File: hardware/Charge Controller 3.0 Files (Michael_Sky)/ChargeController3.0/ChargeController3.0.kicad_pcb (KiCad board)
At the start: 2 copper layers, 95.9 x 90.2 mm, 98 parts, among them J1 Conn_02x26_Odd_Even, J1 Conn_02x30_Row_Letter_First, J10 SOL_TEST_01x01_Pin, J11 GND_TEST_01x01_Pin, J12 Conn_02x26_Odd_Even, J13 Conn-1x2, J14 Conn-1x2, J15 Conn-1x2, J17 SCL_MAS_01x01_Pin, J18 SDA_MAS_01x01_Pin, J19 SYS-1x2, J2 Conn_02x30_Row_Letter_First, J2 SP_01x02_Pin, J3 BATT_TEST_01x01_Pin, J4 3.3V_PULLUP_01x02_Pin, J5 BATT_01x02_Pin, J6 Conn-1x2, J7 Conn-1x2, J8 Conn-1x2, J9 SYS_TEST_01x01_Pin, Q1 SI2318CDS-T1-GE3, Q10 SI2318CDS-T1-GE3, Q11 SI2318CDS-T1-GE3, Q13 SI2318CDS-T1-GE3, Q2 SI2318CDS-T1-GE3, Q3 SI2318CDS-T1-GE3, Q4 SI2318CDS-T1-GE3, Q5 AONS66614, Q6 AONS66614, Q7 AONS66614, Q8 AONS66614, Q9 SI2318CDS-T1-GE3, SW1 100SP1T1B1M1QEH, U1 BQ25756ERRVR

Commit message: template layout
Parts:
- removed D6: SS24, bmsfootprints:SS24
- removed the H1 at (38.6, 3.02)
- removed the H1 at (102.8, 59.0)
- removed the H2 at (38.6, 10.1)
- removed the H2 at (188.5, 56.5)
- removed the H3 at (38.6, 17.1)
- removed the H3 at (102.8, 132.7)
- removed the H4 at (38.6, 24.2)
- removed the H4 at (188.5, 136.5)
- removed the J1 at (106.8, 125.1)
- removed the J1 at (73.0, 4.64)
- removed the J2 at (102.8, 125.1)
- removed the J2 at (15.3, 50.7)
- removed the J3 at (10.6, 41.7)
- removed the J4 at (32.4, 32.5)
- removed Q13: SI2318CDS-T1-GE3, bmsfootprints:SI2318CDS-T1-GE3
- added H1: MountingHole_Pad, MountingHole:MountingHole_3.2mm_M3_Pad_TopBottom, F.Cu at (113.6, 53.0)
- added H2: MountingHole_Pad, MountingHole:MountingHole_3.2mm_M3_Pad_TopBottom, F.Cu at (199.3, 56.8)
- added H3: MountingHole_Pad, MountingHole:MountingHole_3.2mm_M3_Pad_TopBottom, F.Cu at (113.6, 133.0)
- added H4: MountingHole_Pad, MountingHole:MountingHole_3.2mm_M3_Pad_TopBottom, F.Cu at (199.3, 130.5)
- added H4: MountingHole_Pad, MountingHole:MountingHole_3.2mm_M3_ISO14580_Pad, F.Cu at (36.3, 79.5)
- added J1: Conn_02x26_Odd_Even, Connector_PinSocket_2.54mm:PinSocket_2x26_P2.54mm_Vertical, F.Cu at (21.3, 18.3)
- added J2: SP_01x02_Pin, Connector_PinHeader_2.54mm:PinHeader_1x02_P2.54mm_Vertical, F.Cu at (49.3, 48.9)
- added J3: BATT_TEST_01x01_Pin, Connector_PinHeader_2.54mm:PinHeader_1x01_P2.54mm_Vertical, F.Cu at (53.7, 57.9)
- added J3: Conn_02x26_Row_Letter_First, Connector_PinSocket_2.54mm:PinSocket_2x26_P2.54mm_Vertical, F.Cu at (194.2, 61.9)
- added J4: Conn_02x26_Row_Letter_First, Connector_PinSocket_2.54mm:PinSocket_2x26_P2.54mm_Vertical, F.Cu at (199.3, 61.9)
- added J4: 3.3V_PULLUP_01x02_Pin, Connector_PinHeader_2.54mm:PinHeader_1x02_P2.54mm_Vertical, F.Cu at (65.1, 48.9)
- moved J6 76.1 mm to (65.1, 75.7)
- moved J7 76.1 mm to (69.7, 75.7)
- moved R24 76.1 mm to (74.5, 81.5)
- moved RT1 76.1 mm to (65.9, 82.4)
- moved R25 76.1 mm to (71.1, 81.8)
- moved R26 76.1 mm to (71.1, 84.3)
- moved J8 76.1 mm to (74.3, 75.7)
- moved J12 55.3 mm to (28.5, 18.3)
- moved D7 47.7 mm to (47.4, 58.2)
- moved D8 47.7 mm to (47.4, 63.4)
- moved D9 47.7 mm to (47.4, 68.6)
- moved J9 46.1 mm to (53.7, 62.5)
- moved J10 46.1 mm to (53.7, 67.1)
- moved J11 46.0 mm to (53.7, 71.7)
- moved Q4 39.8 mm to (35.2, 71.7)
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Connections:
- C12 pad 2: GND -> PGND
- C13 pad 2: GND -> PGND
- C14 pad 1: GND -> PGND
- C16 pad 1: GND -> PGND
- C17 pad 2: GND -> PGND
- C18 pad 2: GND -> PGND
- C2 pad 2: GND -> PGND
- C22 pad 2: GND -> PGND
- C23 pad 2: GND -> PGND
- C24 pad 2: GND -> PGND
- C25 pad 1: GND -> PGND
- C27 pad 1: GND -> PGND
- C3 pad 2: GND -> PGND
- C4 pad 2: GND -> PGND
- C6 pad 2: GND -> PGND
- C7 pad 2: GND -> PGND
- D7 pad A: Net-(D6-PadC) -> Net-(J10-Pin_1)
- J11 pad 1: GND -> PGND
- J12 pad 23: unconnected-(J12-Pin_23-Pad23) -> 3.3V
- J12 pad 24: unconnected-(J12-Pin_24-Pad24) -> 3.3V
- J12 pad 27: unconnected-(J12-Pin_27-Pad27) -> 12V
- J12 pad 28: unconnected-(J12-Pin_28-Pad28) -> 12V
- J12 pad 29: GND -> PGND
- J12 pad 30: GND -> PGND
- J12 pad 31: GND -> PGND
- J12 pad 32: GND -> PGND
- J12 pad 43: unconnected-(J12-Pin_43-Pad43) -> SOL
- J12 pad 45: BATT -> SYS/BATT
- J13 pad 1: GND -> PGND
- J19 pad 2: GND -> PGND
- J8 pad 2: GND -> PGND
- Q1 pad 3: Net-(D6-PadC) -> Net-(J10-Pin_1)
- Q7 pad 1: GND -> PGND
- Q7 pad 2: GND -> PGND
- Q7 pad 3: GND -> PGND
- Q8 pad 1: GND -> PGND
- Q8 pad 2: GND -> PGND
- Q8 pad 3: GND -> PGND
- Q9 pad 3: GND -> PGND
- R24 pad 1: GND -> PGND
- R26 pad 1: GND -> PGND
- R_AC3 pad 2: GND -> PGND
- R_FSW_SYNC1 pad 1: GND -> PGND
- R_ICHG1 pad 1: GND -> PGND
- R_ILIM_HIZ1 pad 1: GND -> PGND
- SW1 pad 3: GND -> PGND
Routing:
- added copper zone on B.Cu, net GND
- added copper zone on F.Cu, net GND

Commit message: pcb template start
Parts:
- removed the J3 at (194.2, 61.9)
- removed the J4 at (199.3, 61.9)
- moved J1 177.3 mm to (189.7, 73.9)
- moved J12 175.4 mm to (194.8, 73.9)
- moved L1 108.2 mm to (124.4, 105.5)
- moved H1 12.8 mm to (109.1, 65.0)
- moved H2 12.8 mm to (194.8, 68.8)
- moved H3 12.8 mm to (109.1, 145.0)
- moved H4 12.8 mm to (194.8, 142.5)
- moved Q1 8.34 mm to (26.9, 57.0)
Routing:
- removed copper zone on B.Cu, net GND
- removed copper zone on F.Cu, net GND
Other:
- board text removed: "A1"
- board text removed: "A30"
- board text removed: "B"
- board text removed: "C"
- board text removed: "D1"
- board text removed: "D30"

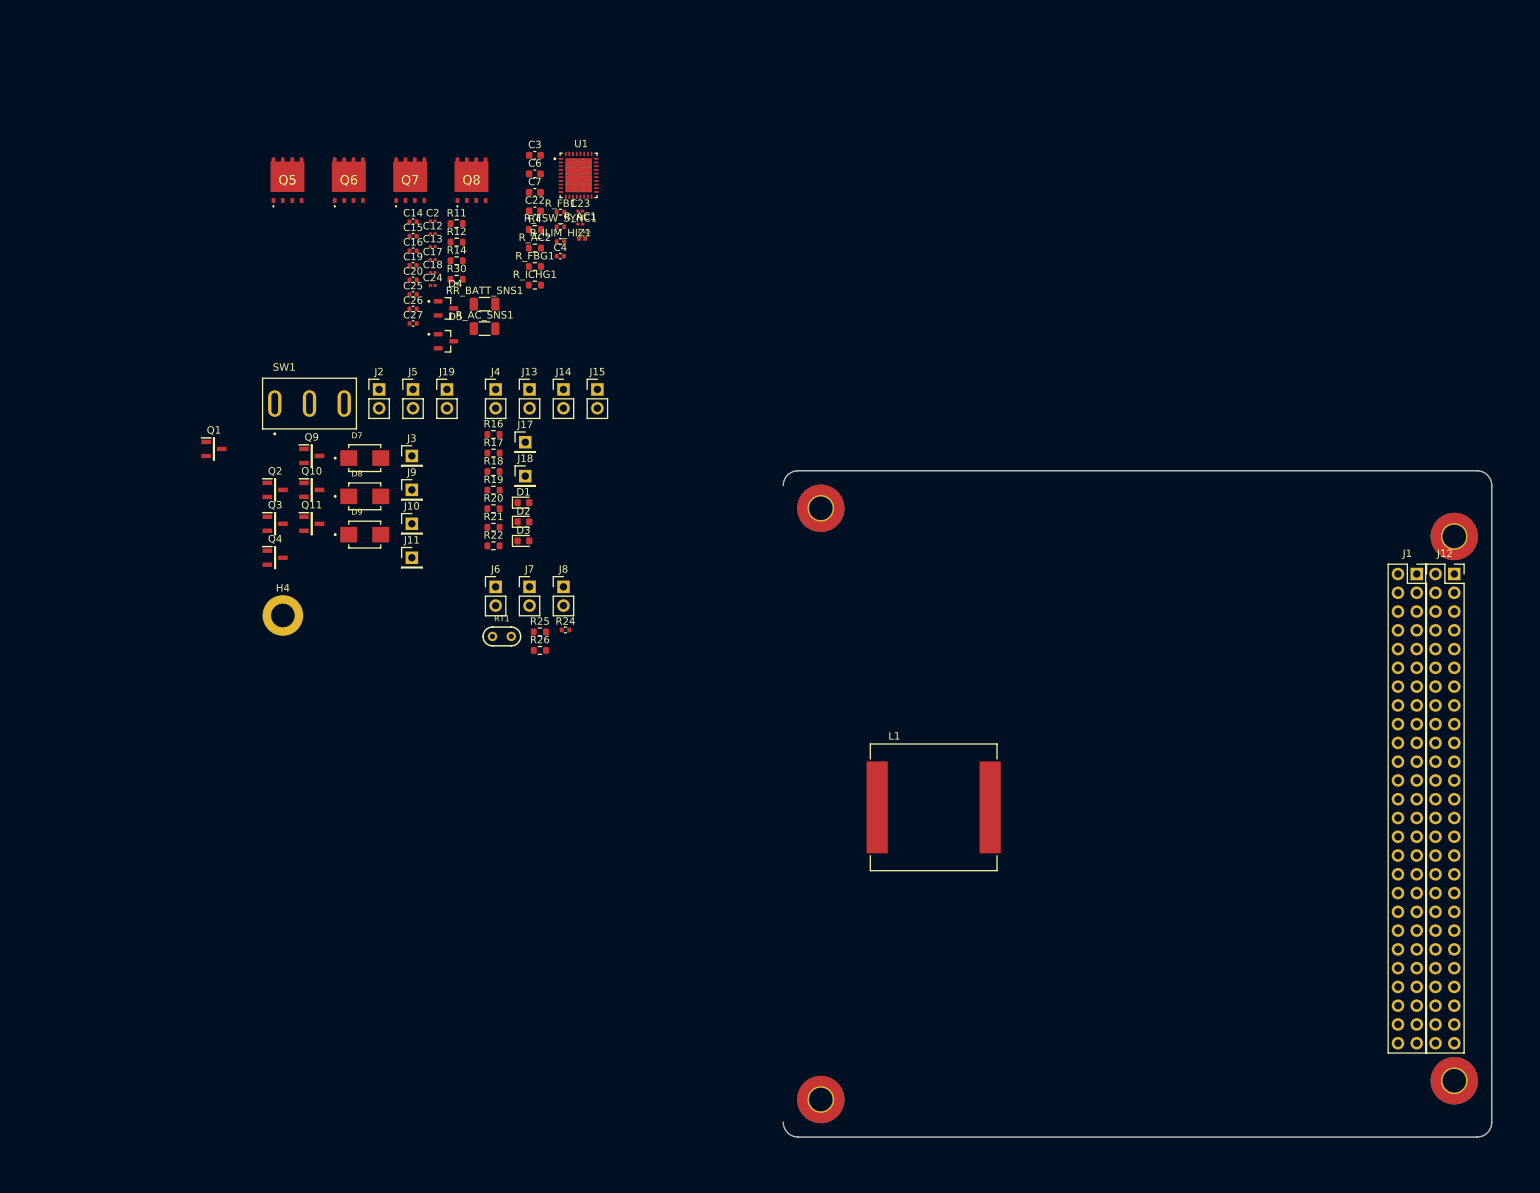
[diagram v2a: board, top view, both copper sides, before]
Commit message: Added template, reassigned pins
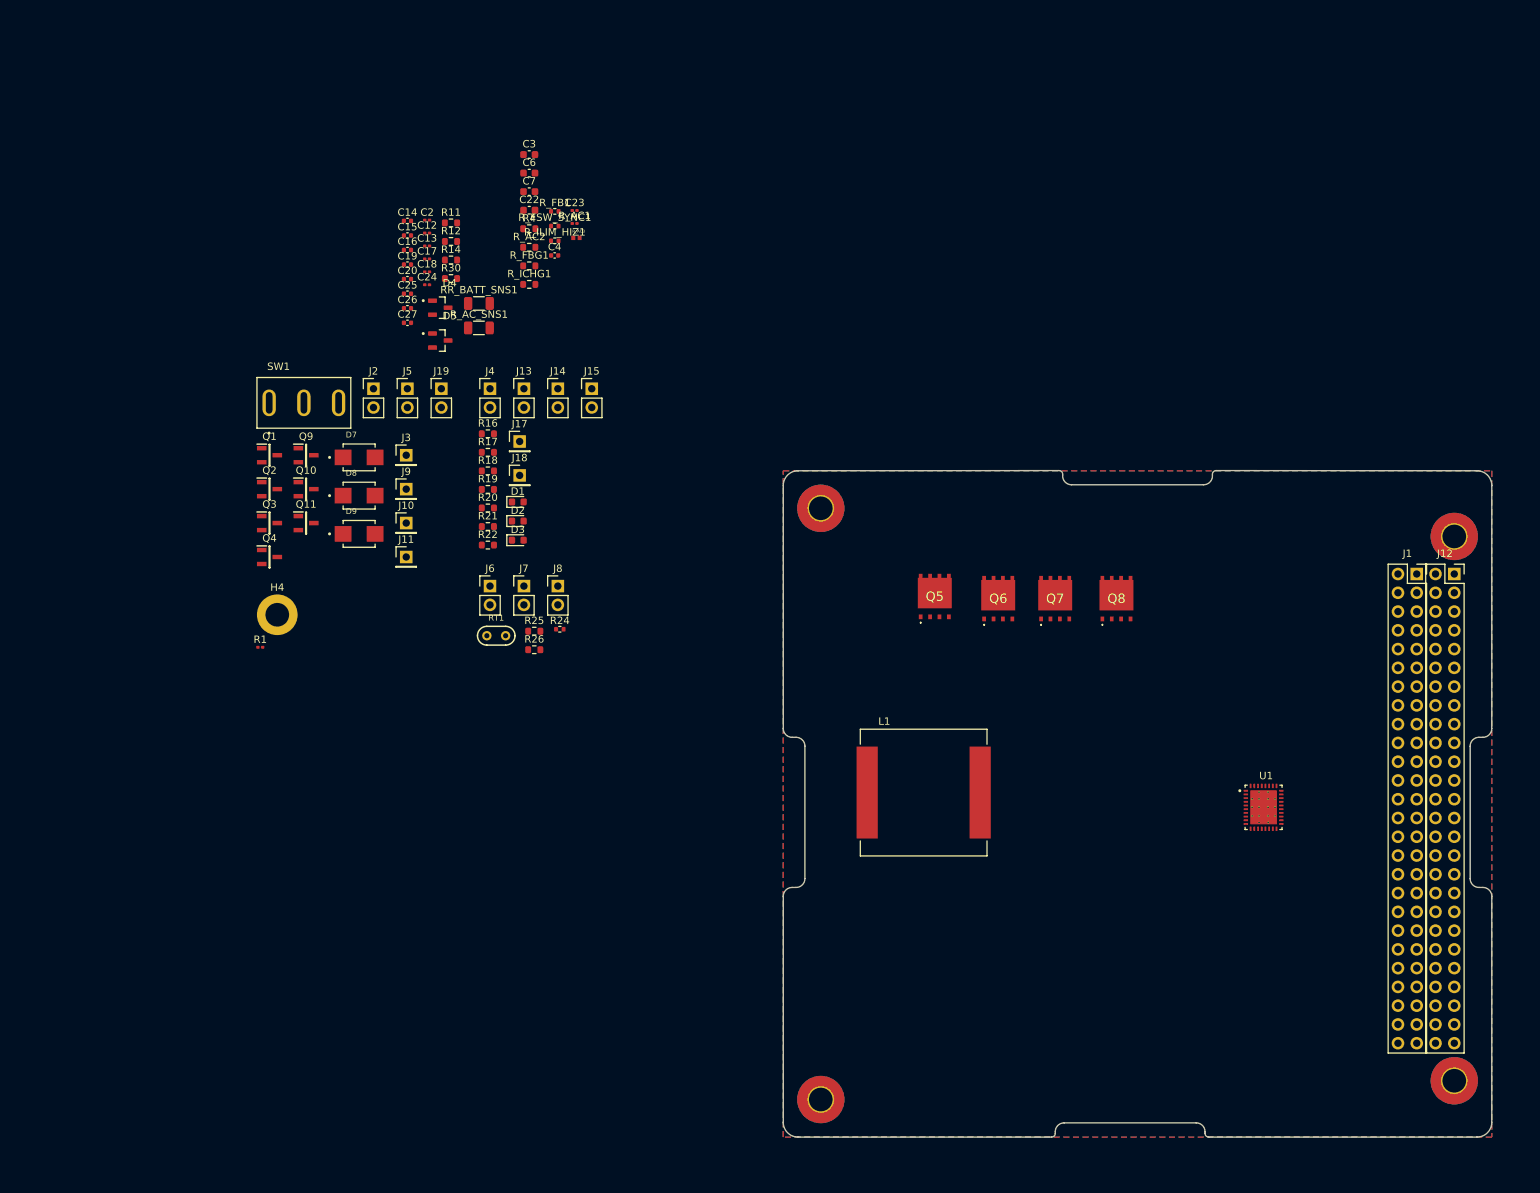
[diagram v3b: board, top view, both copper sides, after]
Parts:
- added R1: 1M, Resistor_SMD:R_0201_0603Metric, F.Cu at (33.2, 83.8)
- moved U1 126.1 mm to (169.0, 105.5)
- moved Q6 104.5 mm to (133.1, 77.2)
- moved Q5 104.1 mm to (124.5, 77.0)
- moved Q7 104.0 mm to (140.8, 77.2)
- moved Q8 104.0 mm to (149.1, 77.2)
- moved Q1 7.57 mm to (34.5, 57.8)
- moved L1 2.42 mm to (123.0, 103.5)
- moved R24 0.77 mm to (73.8, 81.4)
- moved RT1 0.77 mm to (65.2, 82.3)
- moved J13 0.77 mm to (68.9, 48.8)
- moved J4 0.77 mm to (64.3, 48.8)
- moved J5 0.77 mm to (53.1, 48.8)
- moved R_ICHG1 0.77 mm to (69.6, 34.7)
- moved C22 0.77 mm to (69.6, 24.7)
- moved C23 0.77 mm to (75.8, 24.7)
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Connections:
- J1 pad 22: unconnected-(J1-Pin_22-Pad22) -> RS-485 SYS1 B
- J1 pad 24: unconnected-(J1-Pin_24-Pad24) -> RS-485 SYS1 B
- J1 pad 39: unconnected-(J1-Pin_39-Pad39) -> RS SYS2 Rx
- J1 pad 40: unconnected-(J1-Pin_40-Pad40) -> RS SYS2 Tx
- J12 pad 23: 3.3V -> 12V
- J12 pad 24: 3.3V -> 12V
- J12 pad 27: 12V -> 3.3V
- J12 pad 28: 12V -> 3.3V
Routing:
- added copper zone on B.Cu, net GND
- added copper zone on F.Cu, net GND
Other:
- outline, holes or cut-outs redrawn

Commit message: New formatting
New formatting
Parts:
- removed the H4 at (194.8, 142.5)
- removed J13, J14, J15, J6, J7, J8: Conn-1x2, Connector_PinHeader_2.54mm:PinHeader_1x02_P2.54mm_Vertical
- removed R18, R26: 10k, Resistor_SMD:R_0603_1608Metric
- added C1: 100nF, Capacitor_SMD:C_0402_1005Metric, F.Cu at (189.0, 144.0)
- added J20: Conn_01x08_Pin, Connector_PinHeader_2.54mm:PinHeader_1x08_P2.54mm_Horizontal, F.Cu at (160.2, 145.5)
- C12, C13, C17, C18, C2, C24: footprint Capacitor_SMD:C_0201_0603Metric -> bmsfootprints:CAP_UCD_6P3X7P7_NCH
- H1, H2, H3: value MountingHole_Pad -> MountingHole; footprint MountingHole:MountingHole_3.2mm_M3_Pad_TopBottom -> MountingHole:MountingHole_3.2mm_M3_ISO14580
- moved H4 171.3 mm to (194.8, 142.5)
- moved R1 170.0 mm to (191.3, 146.2), turned to 180 degrees
- moved D7 154.4 mm to (178.6, 138.2)
- moved D8 153.0 mm to (176.0, 145.0)
- moved J5 152.9 mm to (181.4, 132.0), turned to -90 degrees
- moved J10 151.9 mm to (183.2, 145.2)
- moved J2 151.7 mm to (181.5, 121.9), turned to -90 degrees
- moved Q1 150.8 mm to (171.2, 121.5)
- moved Q4 149.2 mm to (168.3, 137.4)
- moved Q9 146.7 mm to (162.3, 138.0)
- moved J19 146.4 mm to (181.5, 127.0), turned to -90 degrees
- moved Q2 142.7 mm to (165.2, 119.8)
- moved D9 142.5 mm to (166.8, 145.0)
- moved Q3 138.3 mm to (154.9, 135.0)
- moved Q10 136.5 mm to (158.8, 128.6), turned to 90 degrees
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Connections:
- C12 pad 2: PGND -> GND
- C13 pad 1: SOL -> IN
- C13 pad 2: PGND -> GND
- C14 pad 1: PGND -> GND
- C16 pad 1: PGND -> GND
- C17 pad 1: SYS/BATT -> OUT
- C17 pad 2: PGND -> GND
- C18 pad 1: SYS/BATT -> OUT
- C18 pad 2: PGND -> GND
- C2 pad 1: SOL -> IN
- C2 pad 2: PGND -> GND
- C22 pad 2: PGND -> GND
- C23 pad 1: SOL -> IN
- C23 pad 2: PGND -> GND
- C24 pad 2: PGND -> GND
- C25 pad 1: PGND -> GND
- C27 pad 1: PGND -> GND
- C3 pad 2: PGND -> GND
- C4 pad 1: SOL -> IN
- C4 pad 2: PGND -> GND
- C6 pad 2: PGND -> GND
- C7 pad 1: SOL -> IN
- C7 pad 2: PGND -> GND
- D2 pad 1: Net-(D2-K) -> STAT_1
- D7 pad A: Net-(J10-Pin_1) -> SOL_PIN
- D8 pad A: SYS/BATT -> BATT_PIN
- J1 pad 10: SCL -> PG
- J1 pad 12: SDA -> INT
- J1 pad 16: STAT_2 -> SDA
- J1 pad 18: PG -> SCL
- J1 pad 20: CE -> unconnected-(J1-Pin_20-Pad20)
- J1 pad 33: PGND -> GND
- J1 pad 34: PGND -> GND
- J1 pad 42: unconnected-(J1-Pin_42-Pad42) -> UART_RX
- J1 pad 44: unconnected-(J1-Pin_44-Pad44) -> UART_TX
- J1 pad 9: INT -> STAT_2
- J10 pad 1: Net-(J10-Pin_1) -> SOL_PIN
- J11 pad 1: PGND -> GND
- J12 pad 29: PGND -> GND
- J12 pad 30: PGND -> GND
- J12 pad 31: PGND -> GND
- J12 pad 32: PGND -> GND
- J12 pad 43: SOL -> SOL_PIN
- J12 pad 44: SOL -> SOL_PIN
- J12 pad 45: SYS/BATT -> BATT_PIN
- J12 pad 46: SYS/BATT -> SYS_PIN
- J12 pad 47: unconnected-(J12-Pin_47-Pad47) -> BATT_PIN
- J12 pad 48: unconnected-(J12-Pin_48-Pad48) -> SYS_PIN
- J19 pad 1: Net-(J19-Pin_1) -> SYS_PIN
- J19 pad 2: PGND -> GND
- J2 pad 1: Net-(J10-Pin_1) -> SOL_PIN
- J2 pad 2: PGND -> GND
- J3 pad 1: SYS/BATT -> BATT_PIN
- J4 pad 1: Net-(J4-Pin_1) -> 3.3V
- J4 pad 2: PGND -> GND
- J5 pad 1: SYS/BATT -> BATT_PIN
- J9 pad 1: Net-(J19-Pin_1) -> SYS_PIN
- Q1 pad 1: /Inhibits, Inputs/EN -> EN
- Q1 pad 3: Net-(J10-Pin_1) -> SOL_PIN
- Q10 pad 1: /Inhibits, Inputs/EN -> EN
- Q10 pad 2: Net-(Q10-Pad2) -> SYS_PIN
- Q10 pad 3: Net-(J19-Pin_1) -> Net-(Q10-Pad3)
- Q11 pad 1: /Inhibits, Inputs/EN -> EN
- Q11 pad 2: Net-(Q10-Pad2) -> Net-(Q10-Pad3)
- Q11 pad 3: SYS/BATT -> OUT
- Q2 pad 1: /Inhibits, Inputs/EN -> EN
- Q2 pad 2: SOL -> IN
- Q3 pad 1: /Inhibits, Inputs/EN -> EN
- Q3 pad 2: SOL -> OUT
- Q3 pad 3: SYS/BATT -> BATT_PIN
- Q4 pad 1: /Inhibits, Inputs/EN -> EN
- Q7 pad 1: PGND -> GND
- Q7 pad 2: PGND -> GND
- Q7 pad 3: PGND -> GND
- Q8 pad 1: PGND -> GND
- Q8 pad 2: PGND -> GND
- Q8 pad 3: PGND -> GND
- Q9 pad 1: /Inhibits, Inputs/EN -> EN
- Q9 pad 3: PGND -> GND
- R1 pad 2: PGND -> GND
- R11 pad 1: SOL -> IN
- R14 pad 1: SYS/BATT -> OUT
- R16 pad 2: Net-(J4-Pin_1) -> 3.3V
- R17 pad 2: Net-(J4-Pin_1) -> 3.3V
- R19 pad 2: Net-(J4-Pin_1) -> 3.3V
- R20 pad 1: Net-(J14-Pin_2) -> INT
- R20 pad 2: Net-(J4-Pin_1) -> 3.3V
- R21 pad 2: Net-(J4-Pin_1) -> 3.3V
- R22 pad 2: Net-(J4-Pin_1) -> 3.3V
- R24 pad 1: PGND -> GND
- R25 pad 2: Net-(J7-Pin_2) -> DRV_SUP
- R4 pad 1: SOL -> IN
- RR_BATT_SNS1 pad 1: SYS/BATT -> OUT
- RT1 pad 2: Net-(J8-Pin_1) -> GND
- R_AC1 pad 1: SOL -> IN
- R_AC3 pad 2: PGND -> GND
- R_AC_SNS1 pad 2: SOL -> IN
- R_FB1 pad 1: SYS/BATT -> BATT_PIN
- R_FSW_SYNC1 pad 1: PGND -> GND
- R_ICHG1 pad 1: PGND -> GND
- R_ILIM_HIZ1 pad 1: PGND -> GND
- SW1 pad 1: /Inhibits, Inputs/EN -> Net-(D7-PadC)
- SW1 pad 2: Net-(D7-PadC) -> EN
- SW1 pad 3: PGND -> GND
- U1 pad 17: PGND -> GND
- U1 pad 22: PGND -> GND
- U1 pad 32: SOL -> IN
- U1 pad 33: SOL -> IN
- U1 pad 37: PGND -> GND
- U1 pad 7: CE -> GND
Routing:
- net BATT_PIN: track 0.00 -> 169.6 mm
- net OUT: track 0.00 -> 149.2 mm
- net GND: track 0.00 -> 100.8 mm, vias 0 -> 35
- net EN: track 0.00 -> 78.5 mm, vias 0 -> 4
- net UART_TX: track 0.00 -> 63.4 mm, vias 0 -> 6
- net UART_RX: track 0.00 -> 62.5 mm, vias 0 -> 8
- net IN: track 0.00 -> 59.4 mm
- net SYS_PIN: track 0.00 -> 56.7 mm, vias 0 -> 2
- net DRV_SUP: track 0.00 -> 55.4 mm, vias 0 -> 4
- net 3.3V: track 0.00 -> 52.5 mm, vias 0 -> 5
- net Net-(D7-PadC): track 0.00 -> 51.5 mm
- net SOL_PIN: track 0.00 -> 48.2 mm, vias 0 -> 2
- net SW1: track 0.00 -> 42.1 mm
- net SCL: track 0.00 -> 36.7 mm, vias 0 -> 2
- net SW2: track 0.00 -> 36.6 mm, vias 0 -> 2
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- removed copper zone on F.Cu, net GND
